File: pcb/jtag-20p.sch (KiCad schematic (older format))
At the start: 0 parts

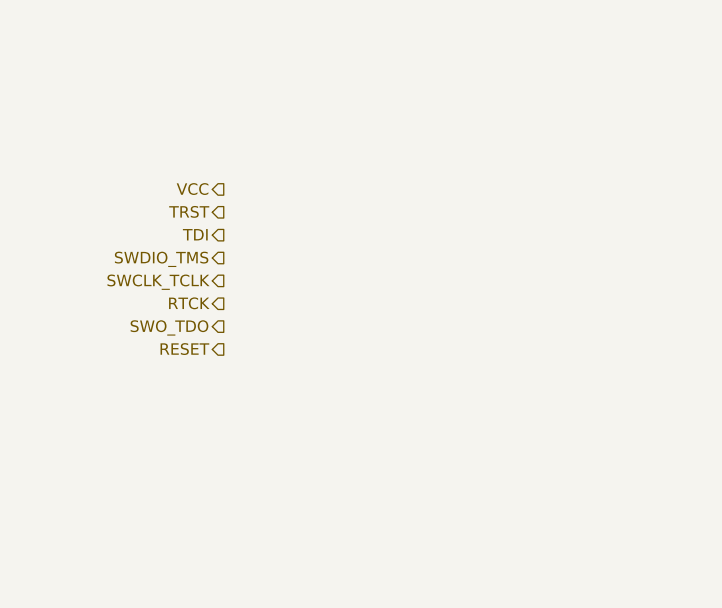
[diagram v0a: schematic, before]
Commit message: SCH: missing signal logic and level shifting
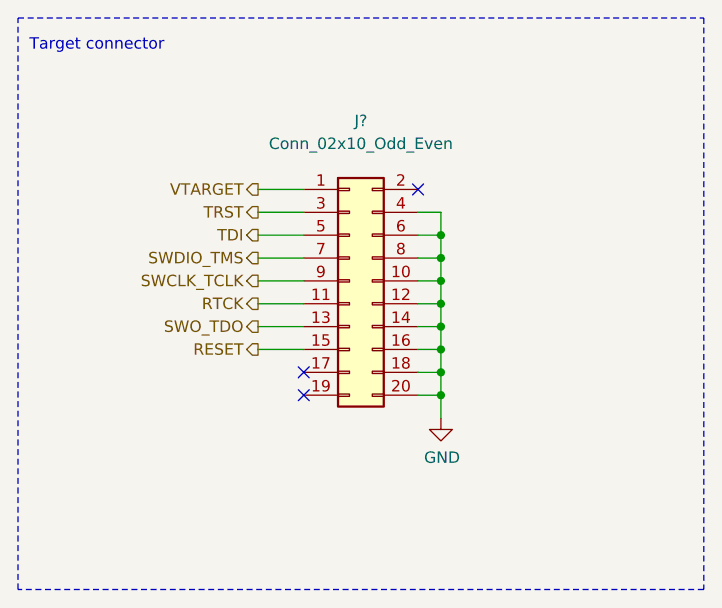
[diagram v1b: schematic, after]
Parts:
- added J?: Conn_02x10_Odd_Even, symbol Connector_Generic:Conn_02x10_Odd_Even
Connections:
- net RESET: now also J?.15 (Pin_15)
- net RTCK: now also J?.11 (Pin_11)
- net SWCLK_TCLK: now also J?.9 (Pin_9)
- net SWDIO_TMS: now also J?.7 (Pin_7)
- net SWO_TDO: now also J?.13 (Pin_13)
- net TDI: now also J?.5 (Pin_5)
- net TRST: now also J?.3 (Pin_3)
- new net GND: J?.10 (Pin_10), J?.12 (Pin_12), J?.14 (Pin_14), J?.16 (Pin_16), J?.18 (Pin_18), J?.20 (Pin_20), J?.4 (Pin_4), J?.6 (Pin_6), J?.8 (Pin_8)
- new net VTARGET: J?.1 (Pin_1)
- no-connect marks 0 -> 3
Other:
- note added: "Target connector"
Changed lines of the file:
@@
 $Descr A4 11693 8268
 encoding utf-8
-Sheet 5 8
-Title ""
-Date ""
-Rev ""
-Comp ""
-Comment1 ""
+Sheet 4 7
+Title "Modular-programmer"
+Date "2020-03-03"
+Rev "1.0"
+Comp "Pepetech"
+Comment1 "Creative Commons Attribution-ShareAlike 4.0 International License"
 Comment2 ""
-Comment3 ""
-Comment4 ""
+Comment3 "Co-designer: João Silva"
+Comment4 "Designer: Rafael Silva"
 $EndDescr
-Text HLabel 3900 3250 0    50   Output ~ 0
-VCC
-Text HLabel 3900 3350 0    50   Output ~ 0
+Text HLabel 4050 3250 0    50   Output ~ 0
+VTARGET
+Text HLabel 4050 3350 0    50   Output ~ 0
 TRST
-Text HLabel 3900 3450 0    50   Output ~ 0
+Text HLabel 4050 3450 0    50   Output ~ 0
 TDI
-Text HLabel 3900 3550 0    50   Output ~ 0
+Text HLabel 4050 3550 0    50   Output ~ 0
 SWDIO_TMS
-Text HLabel 3900 3650 0    50   Output ~ 0
+Text HLabel 4050 3650 0    50   Output ~ 0
 SWCLK_TCLK
-Text HLabel 3900 3750 0    50   Output ~ 0
+Text HLabel 4050 3750 0    50   Output ~ 0
 RTCK
-Text HLabel 3900 3850 0    50   Output ~ 0
+Text HLabel 4050 3850 0    50   Output ~ 0
 SWO_TDO
-Text HLabel 3900 3950 0    50   Output ~ 0
+Text HLabel 4050 3950 0    50   Output ~ 0
 RESET
 $Bitmap
-Pos 7750 3550
+Pos 7700 3700
 Scale 2.000000
 Data
 89 50 4E 47 0D 0A 1A 0A 00 00 00 0D 49 48 44 52 00 00 00 FA 00 00 00 F8 08 02 00 00 00 4A 46 6C
-61 00 00 00 03 73 42 49 54 08 08 08 DB E1 4F E0 00 00 00 09 70 48 59 73 00 00 0B 12 00 00 0B 12
-01 D2 DD 7E FC 00 00 20 00 49 44 41 54 78 9C EC 3D 67 78 55 45 D3 B3 7B DA BD 69 24 10 7A 02 24
+61 00 00 00 03 73 42 49 54 08 08 08 DB E1 4F E0 00 00 00 09 70 48 59 73 00 00 0A F0 00 00 0A F0
+01 42 AC 34 98 00 00 20 00 49 44 41 54 78 9C EC 3D 67 78 55 45 D3 B3 7B DA BD 69 24 10 7A 02 24
 10 20 54 E9 A0 F8 4A 15 04 B1 02 2A 20 16 10 14 14 5F 2C 88 80 8A 88 82 08 22 52 95 22 2A D2 04
 44 01 B1 22 2A 82 54 E9 45 7A 97 9A 90 E4 96 53 76 F7 FB 31 F7 AE 87 04 22 89 BE 10 3E 33 4F 9E
@@
 EndData
 $EndBitmap
+$Comp
+L Connector_Generic:Conn_02x10_Odd_Even J?
+U 1 1 5E6954B5
+P 4450 3650
+F 0 "J?" H 4500 4350 50  0000 C CNN
+F 1 "Conn_02x10_Odd_Even" H 4500 4250 50  0000 C CNN
+F 2 "" H 4450 3650 50  0001 C CNN
+F 3 "~" H 4450 3650 50  0001 C CNN
+	1    4450 3650
+	1    0    0    -1
+$EndComp
+Wire Wire Line
+	4750 3350 4850 3350
+Wire Wire Line
+	4850 3350 4850 3450
+Wire Wire Line
+	4750 4150 4850 4150
+Connection ~ 4850 4150
+Wire Wire Line
+	4850 4150 4850 4250
+Wire Wire Line
+	4750 4050 4850 4050
+Connection ~ 4850 4050
+Wire Wire Line
+	4850 4050 4850 4150
+Wire Wire Line
+	4750 3950 4850 3950
+Connection ~ 4850 3950
+Wire Wire Line
+	4850 3950 4850 4050
+Wire Wire Line
+	4750 3850 4850 3850
+Connection ~ 4850 3850
+Wire Wire Line
+	4850 3850 4850 3950
+Wire Wire Line
+	4750 3750 4850 3750
+Connection ~ 4850 3750
+Wire Wire Line
+	4850 3750 4850 3850
+Wire Wire Line
+	4750 3650 4850 3650
+Connection ~ 4850 3650
+Wire Wire Line
+	4850 3650 4850 3750
+Wire Wire Line
+	4750 3550 4850 3550
+Connection ~ 4850 3550
+Wire Wire Line
+	4850 3550 4850 3650
+Wire Wire Line
+	4750 3450 4850 3450
+Connection ~ 4850 3450
+Wire Wire Line
+	4850 3450 4850 3550
+NoConn ~ 4250 4050
+NoConn ~ 4250 4150
+$Comp
+L power:GND #PWR?
+U 1 1 5E699B1F
+P 4850 4250
+F 0 "#PWR?" H 4850 4000 50  0001 C CNN
+F 1 "GND" H 4855 4077 50  0000 C CNN
+F 2 "" H 4850 4250 50  0001 C CNN
+F 3 "" H 4850 4250 50  0001 C CNN
+	1    4850 4250
+	1    0    0    -1
+$EndComp
+Wire Wire Line
+	4050 3950 4250 3950
+Wire Wire Line
+	4050 3350 4250 3350
+Wire Wire Line
+	4050 3450 4250 3450
+Wire Wire Line
+	4050 3550 4250 3550
+Wire Wire Line
+	4050 3650 4250 3650
+Wire Wire Line
+	4050 3750 4250 3750
+Wire Wire Line
+	4050 3850 4250 3850
+Wire Wire Line
+	4050 3250 4250 3250
+NoConn ~ 4750 3250
+Wire Notes Line
+	3000 2500 6000 2500
+Wire Notes Line
+	6000 2500 6000 5000
+Wire Notes Line
+	6000 5000 3000 5000
+Wire Notes Line
+	3000 5000 3000 2500
+Text Notes 3050 2650 0    50   ~ 0
+Target connector
 $EndSCHEMATC

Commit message: SCH: minor changes
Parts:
- removed J?: Conn_02x10_Odd_Even, symbol Connector_Generic:Conn_02x10_Odd_Even
- added J?: Conn_02x05_Odd_Even, symbol Connector_Generic:Conn_02x05_Odd_Even
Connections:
- net GND: now also J?.3 (Pin_3), J?.5 (Pin_5)
- net RESET: now also J?.10 (Pin_10)
- net RTCK: now also J?.7 (Pin_7)
- net SWCLK_TCLK: now also J?.4 (Pin_4)
- net SWDIO_TMS: now also J?.2 (Pin_2)
- net SWO_TDO: now also J?.6 (Pin_6)
- net TDI: now also J?.8 (Pin_8)
- net TRST: now also J?.9 (Pin_9)
- net VTARGET: now also J?.1 (Pin_1)
- no-connect marks 3 -> 0
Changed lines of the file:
@@
 Comment4 "Designer: Rafael Silva"
 $EndDescr
-Text HLabel 4050 3250 0    50   Output ~ 0
+Text HLabel 4050 3550 0    50   Output ~ 0
 VTARGET
-Text HLabel 4050 3350 0    50   Output ~ 0
+Text HLabel 4050 3950 0    50   Output ~ 0
 TRST
-Text HLabel 4050 3450 0    50   Output ~ 0
+Text HLabel 4950 3850 2    50   Output ~ 0
 TDI
-Text HLabel 4050 3550 0    50   Output ~ 0
+Text HLabel 4950 3550 2    50   Output ~ 0
 SWDIO_TMS
-Text HLabel 4050 3650 0    50   Output ~ 0
+Text HLabel 4950 3650 2    50   Output ~ 0
 SWCLK_TCLK
-Text HLabel 4050 3750 0    50   Output ~ 0
+Text HLabel 4050 3850 0    50   Output ~ 0
 RTCK
-Text HLabel 4050 3850 0    50   Output ~ 0
+Text HLabel 4950 3750 2    50   Output ~ 0
 SWO_TDO
-Text HLabel 4050 3950 0    50   Output ~ 0
+Text HLabel 4950 3950 2    50   Output ~ 0
 RESET
 $Bitmap
@@
 EndData
 $EndBitmap
-$Comp
-L Connector_Generic:Conn_02x10_Odd_Even J?
-U 1 1 5E6954B5
-P 4450 3650
-F 0 "J?" H 4500 4350 50  0000 C CNN
-F 1 "Conn_02x10_Odd_Even" H 4500 4250 50  0000 C CNN
-F 2 "" H 4450 3650 50  0001 C CNN
-F 3 "~" H 4450 3650 50  0001 C CNN
-	1    4450 3650
-	1    0    0    -1
-$EndComp
 Wire Wire Line
-	4750 3350 4850 3350
-Wire Wire Line
-	4850 3350 4850 3450
-Wire Wire Line
-	4750 4150 4850 4150
-Connection ~ 4850 4150
-Wire Wire Line
-	4850 4150 4850 4250
-Wire Wire Line
-	4750 4050 4850 4050
-Connection ~ 4850 4050
-Wire Wire Line
-	4850 4050 4850 4150
-Wire Wire Line
-	4750 3950 4850 3950
-Connection ~ 4850 3950
-Wire Wire Line
-	4850 3950 4850 4050
-Wire Wire Line
-	4750 3850 4850 3850
-Connection ~ 4850 3850
-Wire Wire Line
-	4850 3850 4850 3950
-Wire Wire Line
-	4750 3750 4850 3750
-Connection ~ 4850 3750
-Wire Wire Line
-	4850 3750 4850 3850
-Wire Wire Line
-	4750 3650 4850 3650
-Connection ~ 4850 3650
-Wire Wire Line
-	4850 3650 4850 3750
-Wire Wire Line
-	4750 3550 4850 3550
-Connection ~ 4850 3550
-Wire Wire Line
-	4850 3550 4850 3650
-Wire Wire Line
-	4750 3450 4850 3450
-Connection ~ 4850 3450
-Wire Wire Line
-	4850 3450 4850 3550
-NoConn ~ 4250 4050
-NoConn ~ 4250 4150
-$Comp
-L power:GND #PWR?
-U 1 1 5E699B1F
-P 4850 4250
-F 0 "#PWR?" H 4850 4000 50  0001 C CNN
-F 1 "GND" H 4855 4077 50  0000 C CNN
-F 2 "" H 4850 4250 50  0001 C CNN
-F 3 "" H 4850 4250 50  0001 C CNN
-	1    4850 4250
-	1    0    0    -1
-$EndComp
+	4950 3950 4750 3950
 Wire Wire Line
 	4050 3950 4250 3950
 Wire Wire Line
-	4050 3350 4250 3350
+	4950 3850 4750 3850
 Wire Wire Line
-	4050 3450 4250 3450
+	4950 3550 4750 3550
 Wire Wire Line
-	4050 3550 4250 3550
-Wire Wire Line
-	4050 3650 4250 3650
-Wire Wire Line
-	4050 3750 4250 3750
+	4950 3650 4750 3650
 Wire Wire Line
 	4050 3850 4250 3850
 Wire Wire Line
-	4050 3250 4250 3250
-NoConn ~ 4750 3250
+	4950 3750 4750 3750
+Wire Wire Line
+	4050 3550 4250 3550
 Wire Notes Line
 	3000 2500 6000 2500
@@
 Text Notes 3050 2650 0    50   ~ 0
 Target connector
+$Comp
+L Connector_Generic:Conn_02x05_Odd_Even J?
+U 1 1 5E73D401
+P 4450 3750
+F 0 "J?" H 4500 4167 50  0000 C CNN
+F 1 "Conn_02x05_Odd_Even" H 4500 4076 50  0000 C CNN
+F 2 "" H 4450 3750 50  0001 C CNN
+F 3 "~" H 4450 3750 50  0001 C CNN
+	1    4450 3750
+	1    0    0    -1
+$EndComp
+Wire Wire Line
+	4250 3650 4150 3650
+$Comp
+L power:GND #PWR?
+U 1 1 5E7406E4
+P 4050 3700
+F 0 "#PWR?" H 4050 3450 50  0001 C CNN
+F 1 "GND" H 4055 3527 50  0000 C CNN
+F 2 "" H 4050 3700 50  0001 C CNN
+F 3 "" H 4050 3700 50  0001 C CNN
+	1    4050 3700
+	0    1    1    0
+$EndComp
+Wire Wire Line
+	4250 3750 4150 3750
+Wire Wire Line
+	4150 3750 4150 3700
+Wire Wire Line
+	4050 3700 4150 3700
+Connection ~ 4150 3700
+Wire Wire Line
+	4150 3700 4150 3650
 $EndSCHEMATC

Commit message: SCH: slight changes
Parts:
- J401: renamed from J?; footprint (none) -> Connector_PinHeader_2.54mm:PinHeader_2x04_P2.54mm_Vertical
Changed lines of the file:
@@
 Target connector
 $Comp
-L Connector_Generic:Conn_02x05_Odd_Even J?
+L Connector_Generic:Conn_02x05_Odd_Even J401
 U 1 1 5E73D401
 P 4450 3750
-F 0 "J?" H 4500 4167 50  0000 C CNN
+F 0 "J401" H 4500 4167 50  0000 C CNN
 F 1 "Conn_02x05_Odd_Even" H 4500 4076 50  0000 C CNN
-F 2 "" H 4450 3750 50  0001 C CNN
+F 2 "Connector_PinHeader_2.54mm:PinHeader_2x04_P2.54mm_Vertical" H 4450 3750 50  0001 C CNN
 F 3 "~" H 4450 3750 50  0001 C CNN
 	1    4450 3750
@@
 	4250 3650 4150 3650
 $Comp
-L power:GND #PWR?
+L power:GND #PWR0401
 U 1 1 5E7406E4
 P 4050 3700
-F 0 "#PWR?" H 4050 3450 50  0001 C CNN
+F 0 "#PWR0401" H 4050 3450 50  0001 C CNN
 F 1 "GND" H 4055 3527 50  0000 C CNN
 F 2 "" H 4050 3700 50  0001 C CNN
